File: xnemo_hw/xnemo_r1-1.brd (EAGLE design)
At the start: 39.8 x 31.3 mm, 36 parts, among them J1 MICRO_USB_B_RECEPT, J2 DM3D_MICRO_SD, J3 HEADER_2X5_0.05_SMD, J4 HEADER_2X5_0.05_THRU, J5 HEADER_2X5_0.05_THRU, U1 LTC3559, U2 L3GD20, U3 STM32F405RG, U5 HMC5883L, U6 ADXL345, X1 TXC_7A_XTAL

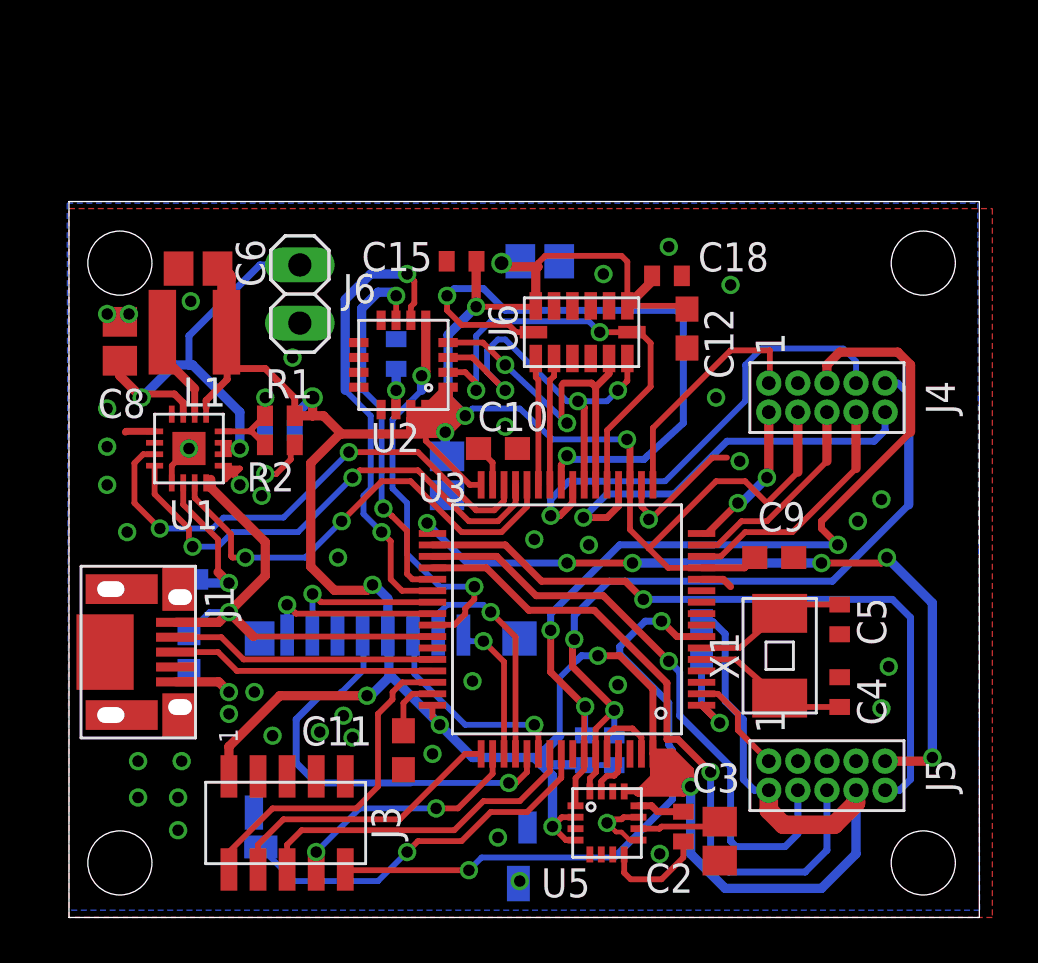
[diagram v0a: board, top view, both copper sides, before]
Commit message: Fixing up R1 schematic for R1A
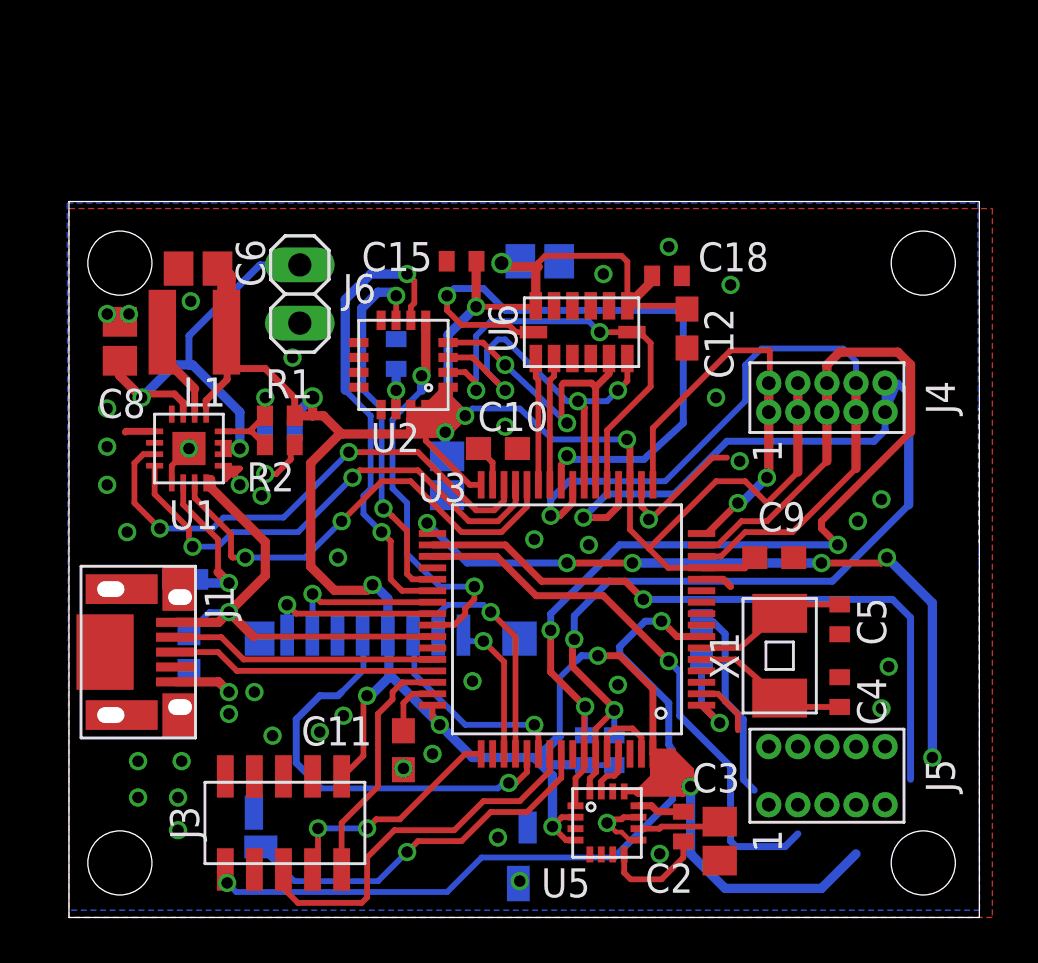
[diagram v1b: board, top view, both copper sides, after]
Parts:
- J5: value HEADER_2X5_0.05_THRU -> HEADER_2X5_0.05X0.1_SMD; device xnemo:HEADER_2X5_0.05_THRU -> xnemo:HEADER_2X5_0.05X0.1_THRU
- moved J3 0.16 mm to (9.37, 4.13), turned to 270 degrees
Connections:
- net JTCK renamed SWCLK
- net JTDO renamed SWO
- net JTMS renamed SWDIO
- net RESET renamed NRESET
- removed net JTDI: J3.8, U3.P$50
- net 3V3: now also J4.4, J5.2, J5.8; no longer J4.P$4, J5.P$2, J5.P$8
- net GND: now also J4.3, J5.3, J5.5, J5.7; no longer J4.P$3, J5.P$3, J5.P$5, J5.P$7
- net I2C_SCL: now also J4.5; no longer J4.P$5
- net I2C_SDA: now also J4.9; no longer J4.P$9
- net PA0: now also J4.8; no longer J4.P$8
- net PA1: now also J4.6; no longer J4.P$6
- net PA2: now also J4.2; no longer J4.P$2
- net PA3: now also J4.1; no longer J4.P$1
- net PA4: now also J4.10; no longer J4.P$10
- net PB12: now also J5.9; no longer J5.P$9
- net PB13: now also J5.10; no longer J5.P$10
- net PB14: now also J5.4; no longer J5.P$4
- net PB15: now also J5.6; no longer J5.P$6
- net PC13: now also J5.1; no longer J5.P$1
- net PC4: now also J4.7; no longer J4.P$7
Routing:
- net PB15: track 29.3 -> 0.00 mm, vias 1 -> 0
- net 3V3: track 191.0 -> 178.7 mm
- net JTDI: track 10.7 -> 0.00 mm, vias 2 -> 0
- net NRESET: track 27.5 -> 33.7 mm
- net SWDIO: track 14.8 -> 10.6 mm
- net SWO: track 14.6 -> 16.9 mm
- net SWCLK: track 12.5 -> 10.5 mm, vias 0 -> 2
- net PC13: track 4.57 -> 2.66 mm
- net PB12: track 33.1 -> 31.2 mm
- net PB14: track 26.4 -> 24.5 mm
- net PB13: track 30.6 -> 29.3 mm
- net PC4: track 20.9 -> 22.1 mm
- net PA4: track 18.2 -> 19.5 mm
- net PA2: track 6.76 -> 8.03 mm
- net PA1: track 9.13 -> 10.4 mm
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
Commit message: I don't remember
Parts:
- added C19: 100n, resistor:C0402
- added C20: 10u, resistor:C0805
- added LED1, LED2: (no value), led:CHIPLED_0603
- added R4: (no value), xnemo:SMD0603
- added R7, R8: (no value), xnemo:SMD0402
- added SW1, SW2: ALPS_SKQG, xnemo:ALPS_SKQG
- added U4: LPS331AP, xnemo:ST_HCLGA-16L
- C14: value 22p -> 10p
- J4: value HEADER_2X5_0.05_THRU -> HEADER_2X5_0.05X0.1_THRU; device xnemo:HEADER_2X5_0.05_THRU -> xnemo:HEADER_2X5_0.05X0.1_THRU
- J5: value HEADER_2X5_0.05X0.1_SMD -> HEADER_2X5_0.05X0.1_THRU
- R1, R2, R3, R5, R6: device resistor:R0402 -> xnemo:SMD0402
- moved J5 30.6 mm to (2.94, 11.1), turned to 0 degrees
- moved R5 10.7 mm to (23.3, 18.0)
- moved R6 10.7 mm to (22.4, 18.0)
- moved R3 9.92 mm to (2.06, 24.2), flipped to the top
- moved C7 8.41 mm to (4.13, 19.9)
- moved J1 8.10 mm to (1.75, 19.7)
- moved U6 7.46 mm to (22.5, 33.0)
- moved C18 7.38 mm to (26.2, 35.4)
- moved C12 7.32 mm to (27.5, 33.0), turned to 0 degrees
- moved C17 6.92 mm to (17.6, 34.9), turned to 0 degrees
- moved J6 6.85 mm to (11.7, 33.9), turned to 180 degrees
- moved R2 6.80 mm to (6.99, 27.1)
- moved U1 6.76 mm to (3.41, 27.0)
- moved C14 6.75 mm to (7.14, 27.7)
- moved J2 6.45 mm to (12.9, 12.8), turned to 0 degrees
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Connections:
- new net 3V3A: R4.P$2, U4.P$15
- new net N$2: LED1.A, R7.P$2
- new net N$3: LED2.A, R8.P$2
- new net PC14: R7.P$1, U3.P$3
- new net PC15: R8.P$1, U3.P$4
- new net SPI_CS_PRS: U4.P$8
- new net USER_BTN: SW2.1_1, U3.P$57
- net 3V3: now also C19.2, C20.1, R1.P$1, R4.P$1, R5.P$1, R6.P$1, U4.P$1, U4.P$14; no longer R1.2, R5.2, R6.2
- net BUCK_FB1: now also R1.P$2, R2.P$1; no longer R1.1, R2.2
- net GND: now also C19.1, C20.2, LED1.C, LED2.C, R2.P$2, R3.P$2, SW1.2_2, SW2.2_2, U4.P$10, U4.P$12, U4.P$13, U4.P$16, U4.P$5; no longer R2.1, R3.2
- net I2C_SCL: now also R6.P$2; no longer R6.1
- net I2C_SDA: now also R5.P$2; no longer R5.1
- net NRESET: now also SW1.1_2
- net POW_PROG: now also R3.P$1; no longer R3.1
- net SPI_CLK: now also U4.P$4
- net SPI_MISO: no longer U2.P$4, U6.P$12
- net SPI_MOSI: now also U4.P$6
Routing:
- net 3V3: track 178.7 -> 123.5 mm, vias 12 -> 11
- net I2C_SCL: track 40.2 -> 0.00 mm, vias 3 -> 0
- net I2C_SDA: track 33.5 -> 0.00 mm, vias 2 -> 0
- net PB12: track 31.2 -> 0.00 mm, vias 6 -> 0
- net PB13: track 29.3 -> 0.00 mm, vias 1 -> 0
- net PB14: track 24.5 -> 0.00 mm, vias 1 -> 0
- net PC4: track 22.1 -> 0.00 mm, vias 1 -> 0
- net PA4: track 19.5 -> 0.00 mm, vias 1 -> 0
- net SD_CLK: track 18.9 -> 0.00 mm, vias 1 -> 0
- net SWO: track 16.9 -> 0.00 mm
- net SD_DET: track 16.7 -> 0.00 mm, vias 1 -> 0
- net SPI_CLK: track 19.4 -> 35.8 mm
- net SPI_MISO: track 15.8 -> 0.00 mm, vias 2 -> 0
- net SPI_MOSI: track 17.7 -> 29.9 mm, vias 3 -> 4
- net PA0: track 12.1 -> 0.00 mm
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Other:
- board size 39.8 x 31.3 mm -> 39.8 x 36.3 mm

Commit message: Routed, now to touch up r1.1
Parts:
- moved C20 4.16 mm to (35.2, 27.6)
- moved C11 3.57 mm to (14.6, 8.81)
- moved J3 3.50 mm to (9.60, 5.71), turned to 0 degrees
- moved C12 3.41 mm to (27.5, 29.6)
- moved U6 3.41 mm to (22.5, 29.6)
- moved C1 3.41 mm to (11.4, 25.0)
- moved C10 3.41 mm to (18.7, 22.1)
- moved C14 3.41 mm to (7.14, 24.3)
- moved C15 3.41 mm to (17.1, 30.3)
- moved C16 3.41 mm to (16.5, 21.0)
- moved C4 3.41 mm to (34.4, 11.9)
- moved C5 3.41 mm to (34.4, 14.4)
- moved C6 3.41 mm to (6.35, 31.2)
- moved C9 3.41 mm to (30.8, 17.4)
- moved J5 3.41 mm to (2.94, 7.70)
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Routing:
- net 3V3: track 123.5 -> 171.5 mm, vias 11 -> 14
- net PC13: track 0.00 -> 45.6 mm
- net I2C_SDA: track 0.00 -> 42.4 mm, vias 0 -> 4
- net SWO: track 0.00 -> 41.7 mm, vias 0 -> 2
- net SD_DAT0: track 0.00 -> 40.5 mm, vias 0 -> 3
- net I2C_SCL: track 0.00 -> 35.4 mm, vias 0 -> 3
- net USER_BTN: track 0.00 -> 32.5 mm, vias 0 -> 2
- net PB13: track 0.00 -> 25.1 mm, vias 0 -> 1
- net PB12: track 0.00 -> 24.9 mm, vias 0 -> 2
- net SD_DAT1: track 0.00 -> 23.5 mm, vias 0 -> 3
- net PB15: track 0.00 -> 21.5 mm, vias 0 -> 4
- net PB14: track 0.00 -> 18.2 mm, vias 0 -> 1
- net SD_DAT3: track 10.1 -> 26.9 mm, vias 1 -> 2
- net PC15: track 0.00 -> 16.7 mm, vias 0 -> 2
- net PC4: track 0.00 -> 15.0 mm, vias 0 -> 2
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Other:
- board size 39.8 x 36.3 mm -> 39.8 x 32.9 mm
- board text added: "xNEMO r1.1"
- board text removed: "xNEMO r1"
